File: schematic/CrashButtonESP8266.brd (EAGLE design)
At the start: 152.4 x 102.6 mm, 15 parts, among them U1 ESP12E_DEVKIT

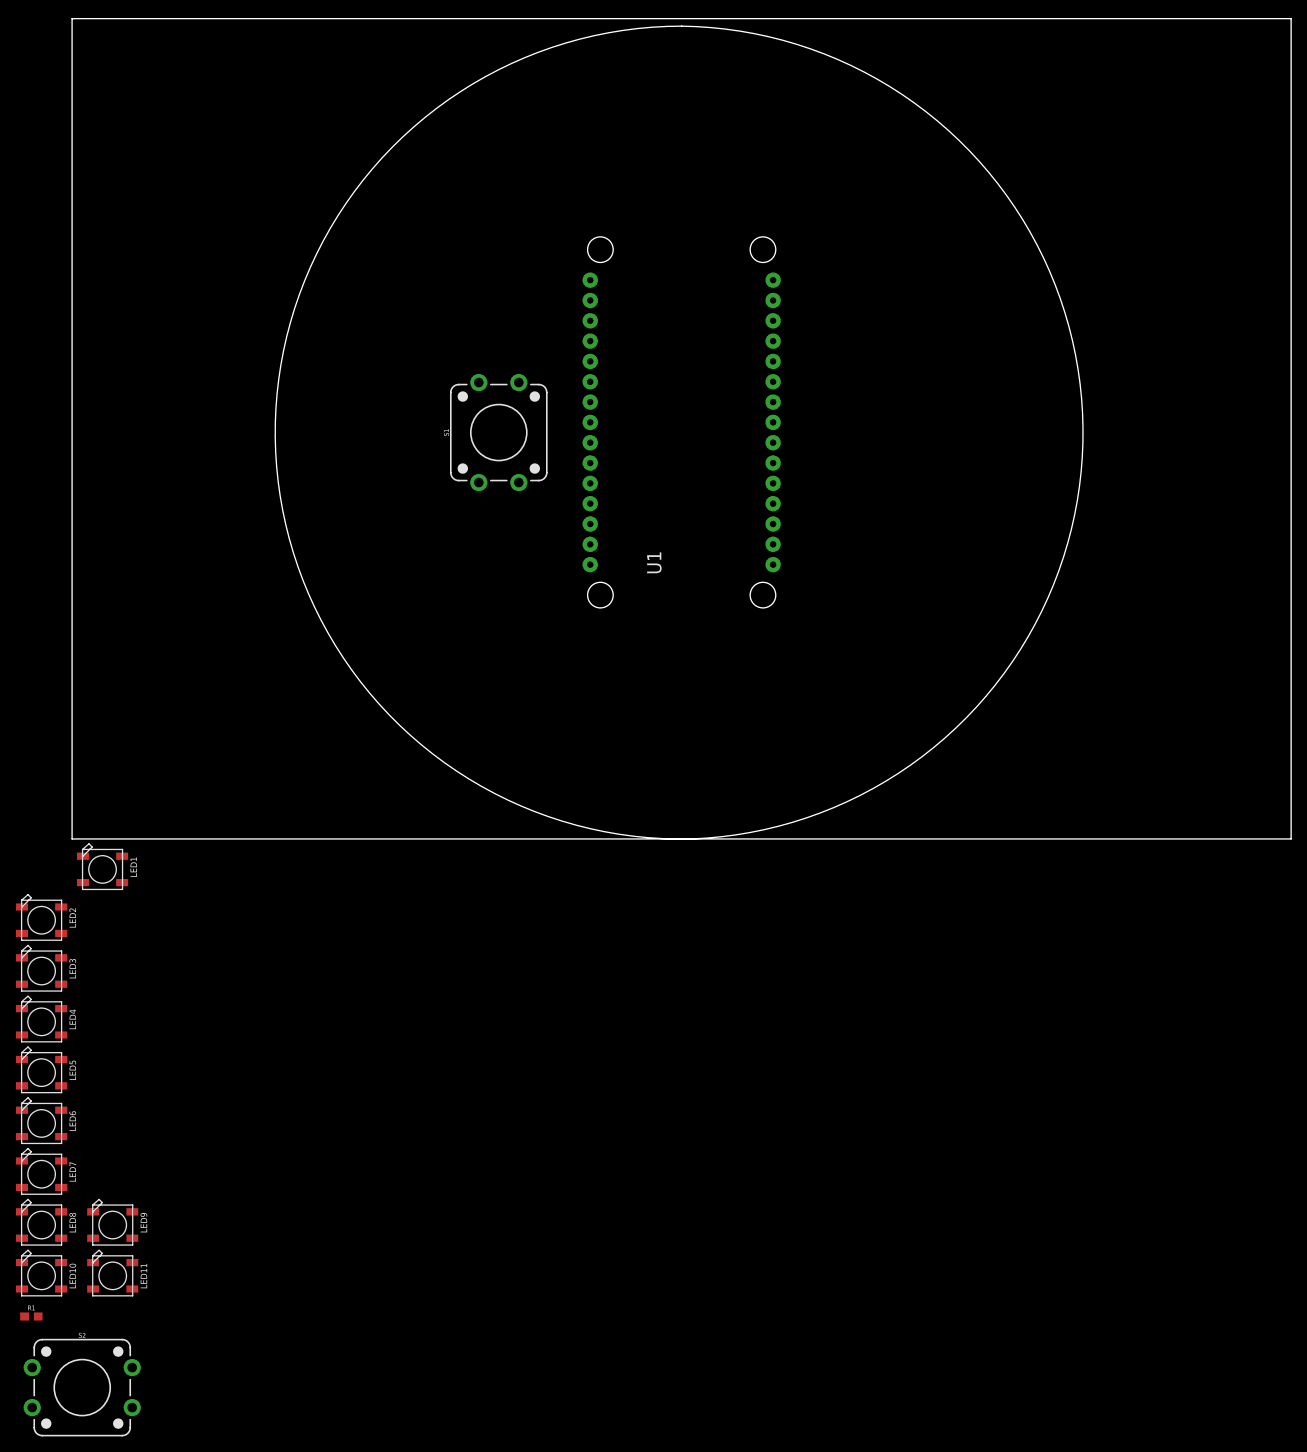
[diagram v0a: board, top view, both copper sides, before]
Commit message: circular layout
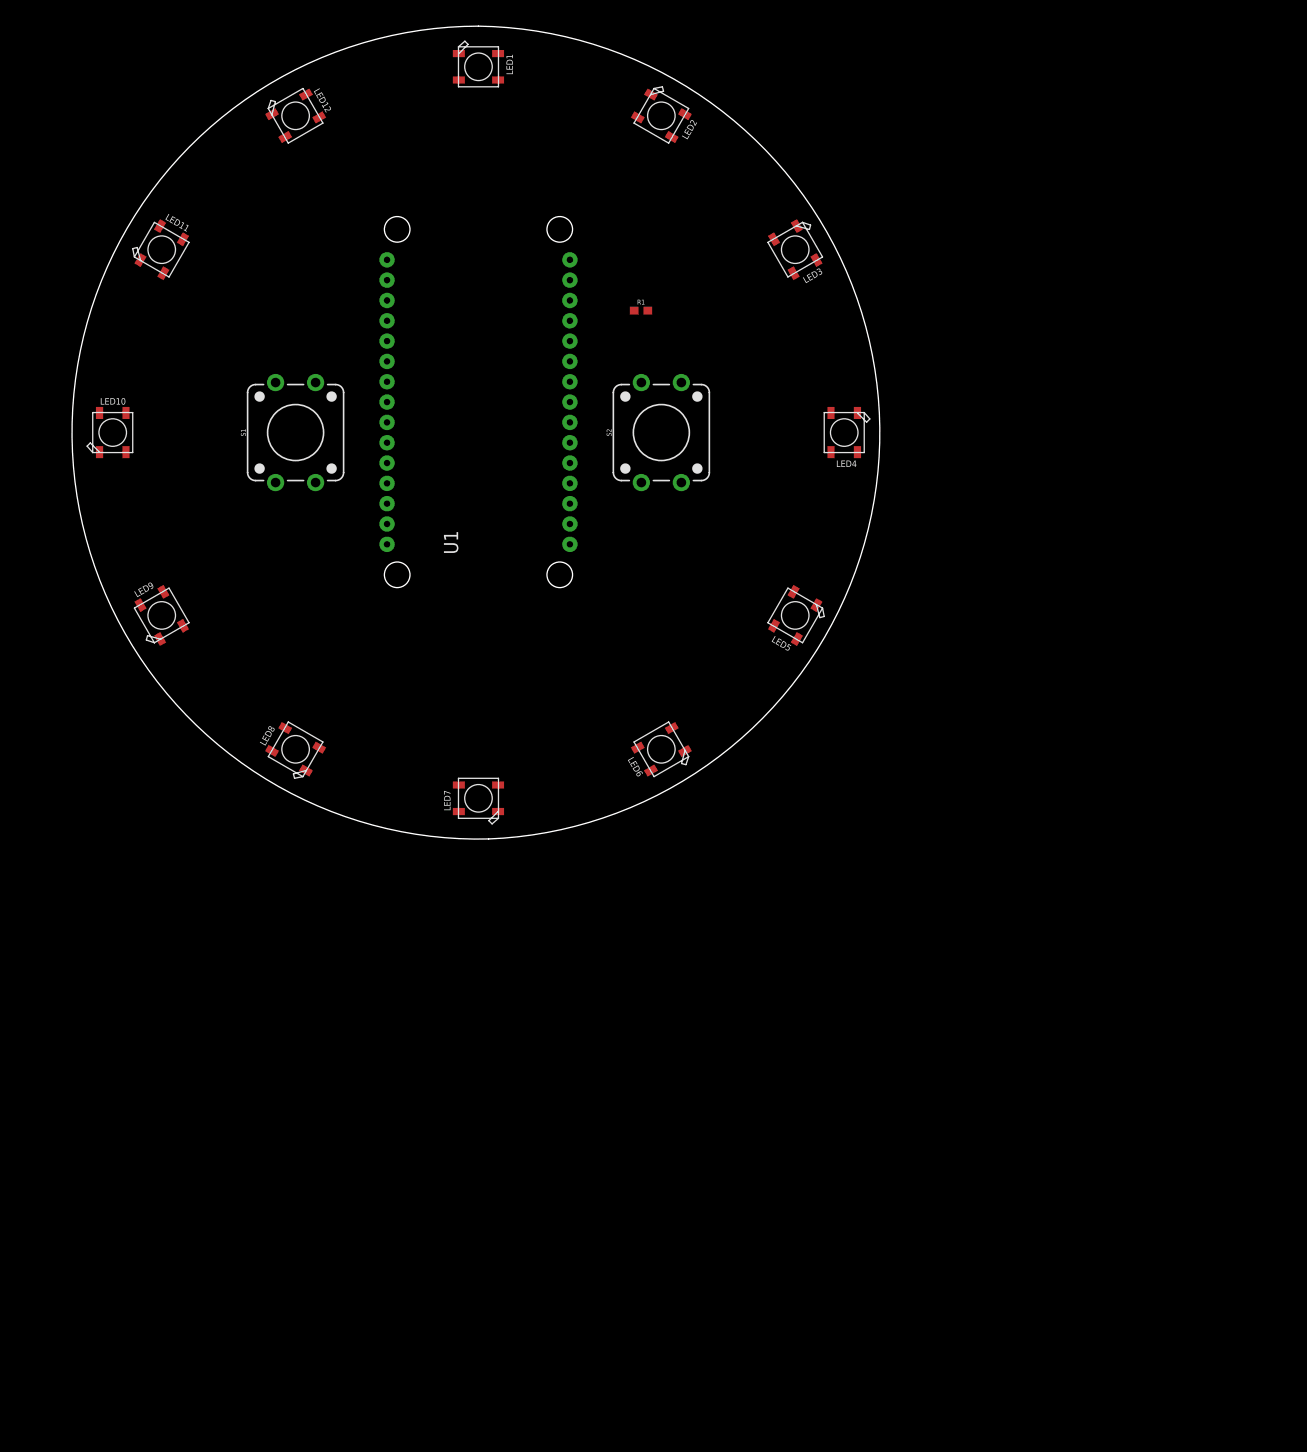
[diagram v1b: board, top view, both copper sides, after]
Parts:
- added LED12: WS2812B5050, adafruit:WS2812B
- moved R1 147.0 mm to (71.1, 66.0)
- moved S2 139.6 mm to (73.7, 50.8), turned to 90 degrees
- moved LED3 130.4 mm to (90.4, 73.7), turned to 300 degrees
- moved LED11 128.4 mm to (11.2, 73.7), turned to 60 degrees
- moved LED2 126.9 mm to (73.7, 90.4), turned to 330 degrees
- moved LED4 124.5 mm to (96.5, 50.8), turned to 270 degrees
- moved LED1 110.8 mm to (50.8, 96.5)
- moved LED5 110.2 mm to (90.4, 27.9), turned to 240 degrees
- moved LED10 105.8 mm to (5.08, 50.8), turned to 90 degrees
- moved LED6 90.5 mm to (73.7, 11.2), turned to 210 degrees
- moved LED9 76.4 mm to (11.2, 27.9), turned to 120 degrees
- moved LED7 72.0 mm to (50.8, 5.08), turned to 180 degrees
- moved LED8 67.4 mm to (27.9, 11.2), turned to 150 degrees
- moved U1 25.5 mm to (50.8, 54.6)
- moved S1 25.4 mm to (27.9, 50.8)
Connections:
- net 5V: now also LED12.1-VDD
- net GND: now also LED12.3-GND
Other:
- board size 152.4 x 102.6 mm -> 101 x 101.6 mm

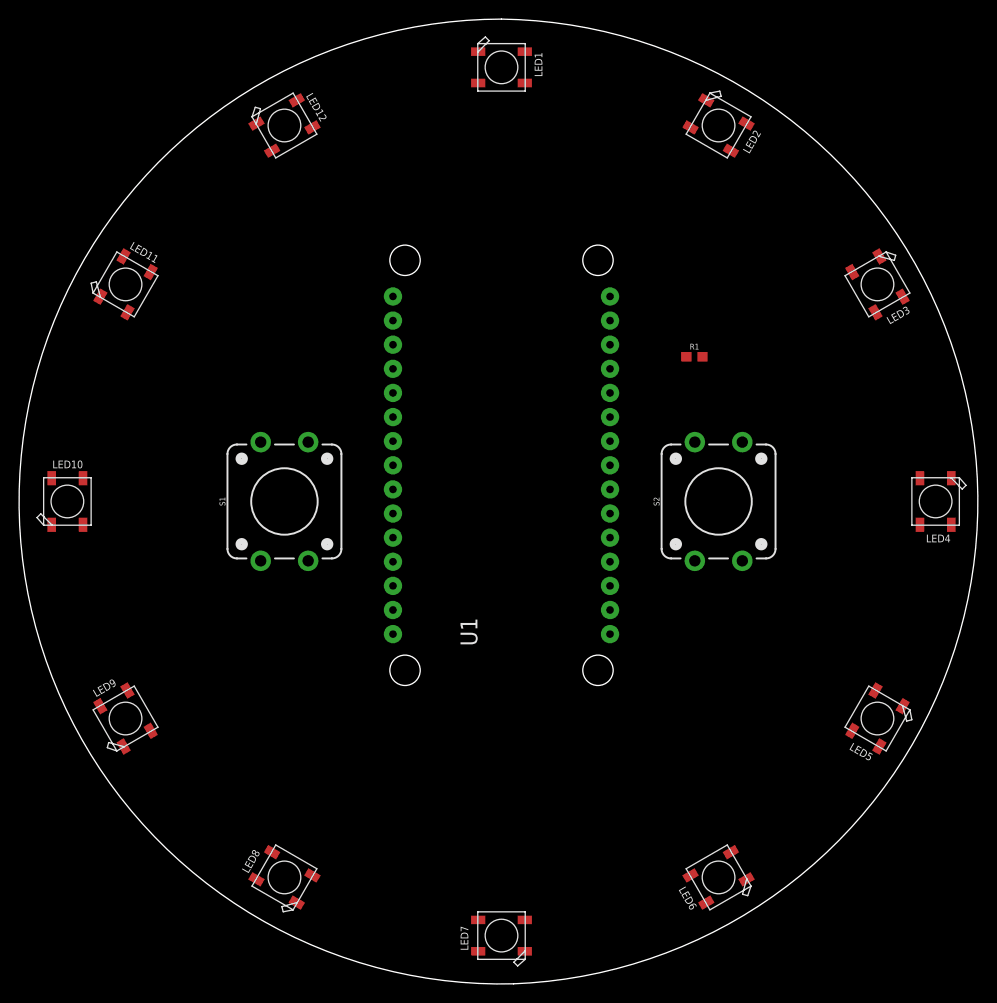
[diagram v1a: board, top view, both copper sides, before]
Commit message: moved buttoncheck to ledticker, moved ledpin to D4 in case I want to use NeoPixelBus
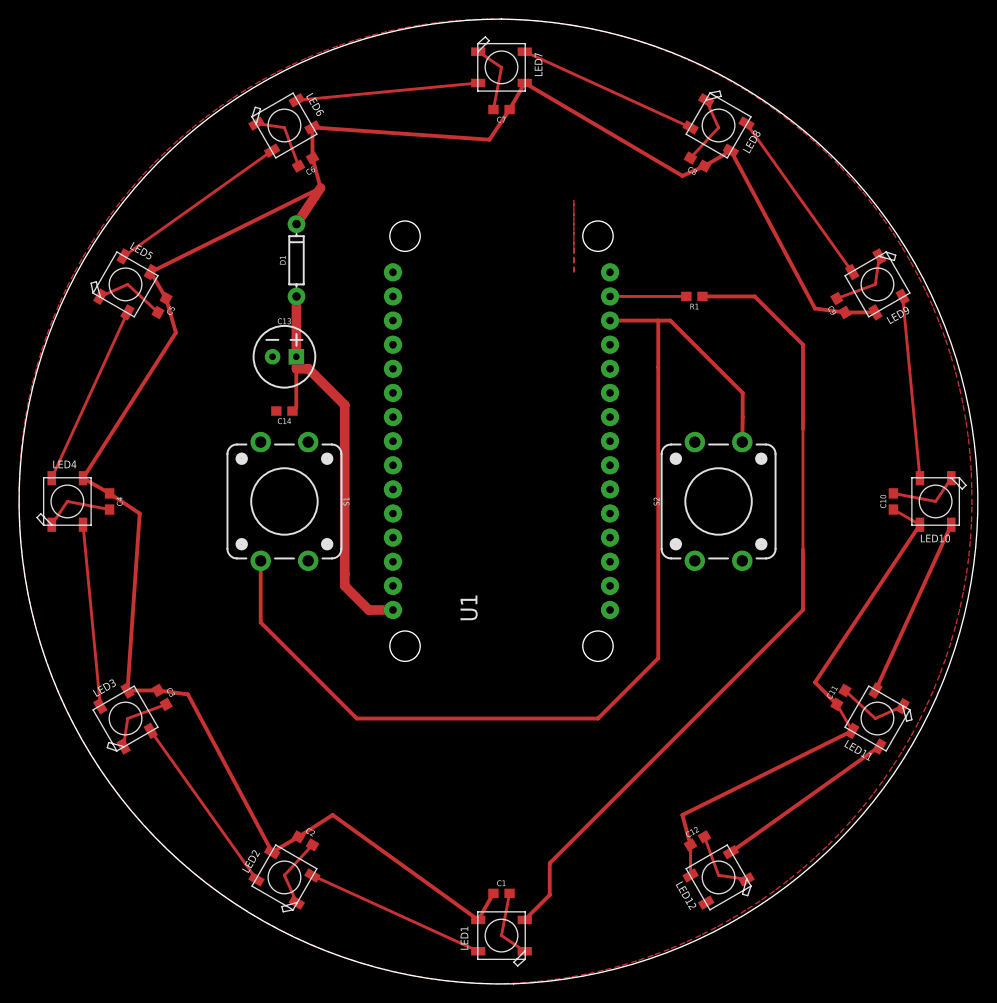
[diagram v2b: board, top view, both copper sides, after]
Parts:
- added C1, C10, C11, C12, C14, C2, C3, C4, C5, C6, C7, C8, C9: 0.1uF, SparkFun-Capacitors:0603
- added C13: 330uF, SparkFun-Capacitors:CPOL-RADIAL-2.5MM-6.5MM
- added D1: 200mA/100V/1V, SparkFun-DiscreteSemi:DIODE-1N4148
- moved LED11 91.4 mm to (90.4, 27.9), turned to 240 degrees
- moved LED12 91.4 mm to (73.7, 11.2), turned to 210 degrees
- moved LED2 91.4 mm to (27.9, 11.2), turned to 150 degrees
- moved LED3 91.4 mm to (11.2, 27.9), turned to 120 degrees
- moved LED5 91.4 mm to (11.2, 73.7), turned to 60 degrees
- moved LED6 91.4 mm to (27.9, 90.4), turned to 30 degrees
- moved LED8 91.4 mm to (73.7, 90.4), turned to 330 degrees
- moved LED9 91.4 mm to (90.4, 73.7), turned to 300 degrees
- moved LED1 91.4 mm to (50.8, 5.08), turned to 180 degrees
- moved LED10 91.4 mm to (96.5, 50.8), turned to 270 degrees
- moved LED4 91.4 mm to (5.08, 50.8), turned to 90 degrees
- moved LED7 91.4 mm to (50.8, 96.5), turned to 0 degrees
- moved R1 6.35 mm to (71.1, 72.4), turned to 180 degrees
- moved U1 2.54 mm to (50.8, 57.1)
- turned S1 to 270 degrees
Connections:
- new net N$12: LED7.2-DOUT, LED8.4-DIN
- new net N$13: LED11.2-DOUT, LED12.4-DIN
- new net N$14: C13.1, C14.1, D1.A, U1.VIN
- new net VCC: C1.1, C2.1, C3.1, C4.1, C5.1, C6.1, C7.1, C8.1, C9.1, D1.C, LED1.1-VDD, LED2.1-VDD, LED3.1-VDD, LED4.1-VDD, LED5.1-VDD, LED6.1-VDD, LED7.1-VDD, LED8.1-VDD, LED9.1-VDD
- net 5V: now also C10.1, C11.1, C12.1; no longer LED1.1-VDD, LED2.1-VDD, LED3.1-VDD, LED4.1-VDD, LED5.1-VDD, LED6.1-VDD, LED7.1-VDD, LED8.1-VDD, LED9.1-VDD, U1.VIN
- net GND: now also C1.2, C10.2, C11.2, C12.2, C13.2, C14.2, C2.2, C3.2, C4.2, C5.2, C6.2, C7.2, C8.2, C9.2
- net LEDDIN: now also R1.1
- net N$10: now also U1.D2
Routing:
- net VCC: track 0.00 -> 212.7 mm
- net N$10: track 0.00 -> 113.8 mm
- net GND: track 0.00 -> 89.1 mm
- net LEDDIN: track 0.00 -> 85.4 mm
- net 5V: track 0.00 -> 56.1 mm
- net N$14: track 0.00 -> 45.3 mm
- net N$5: track 0.00 -> 19.2 mm
- net N$2: track 0.00 -> 19.2 mm
- net N$7: track 0.00 -> 19.2 mm
- net N$13: track 0.00 -> 19.2 mm
- net N$6: track 0.00 -> 19.2 mm
- net N$3: track 0.00 -> 19.2 mm
- net N$9: track 0.00 -> 19.2 mm
- net N$1: track 0.00 -> 19.2 mm
- net N$8: track 0.00 -> 19.2 mm
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- added copper zone on layer 1, net GND
- added copper zone on layer 1, net N$15

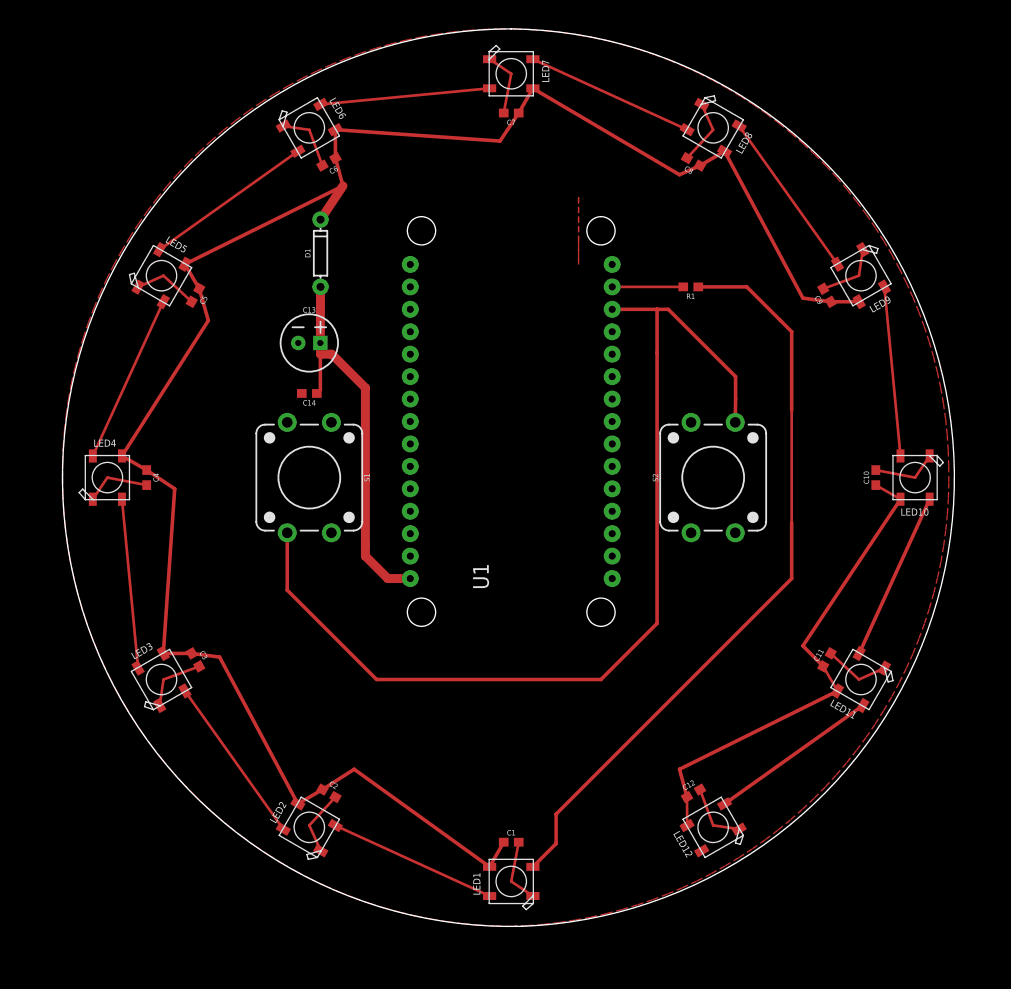
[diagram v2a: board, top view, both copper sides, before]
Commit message: version with enough polygon isolate to be solderable when othermilled
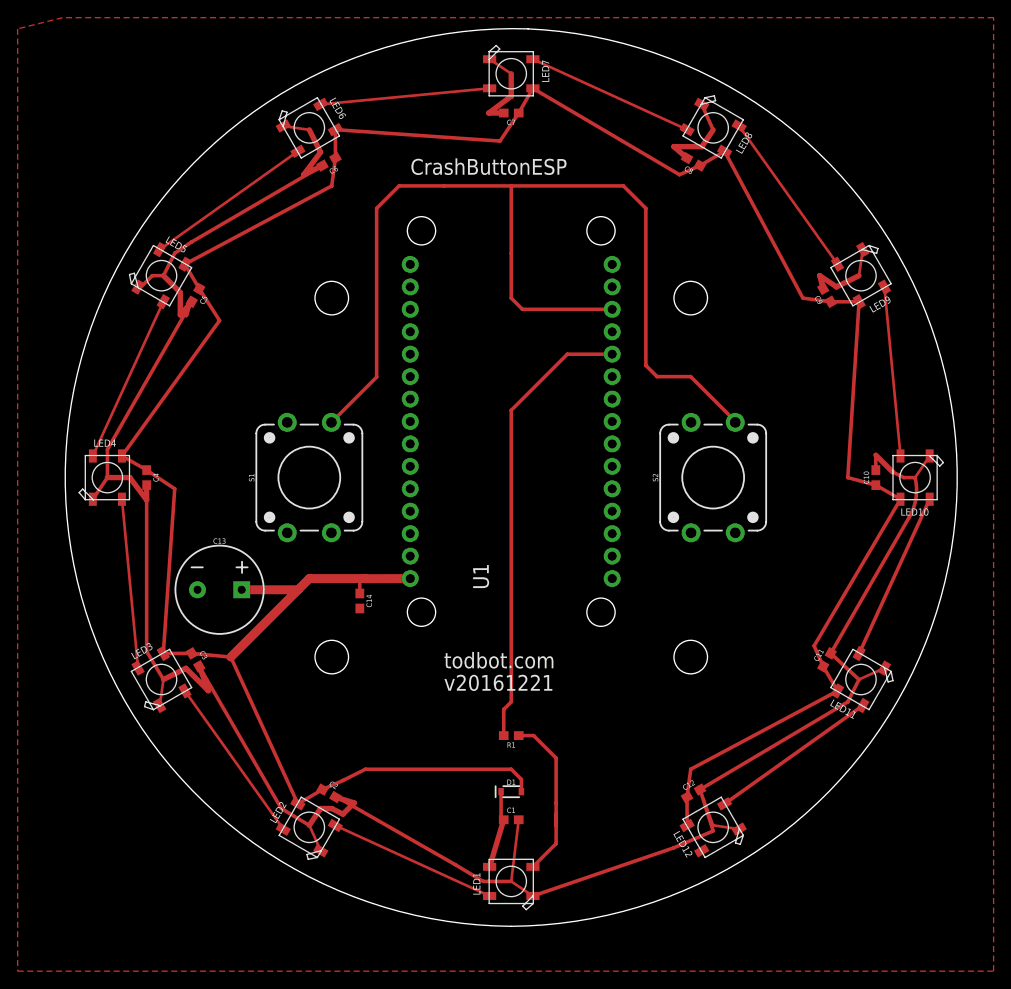
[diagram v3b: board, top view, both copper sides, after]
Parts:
- C13: value 330uF -> 1mF; device SparkFun-Capacitors:CPOL-RADIAL-2.5MM-6.5MM -> SparkFun-Capacitors:CPOL-RADIAL-5MM-10MM
- D1: value 200mA/100V/1V -> 250mA/100V; device SparkFun-DiscreteSemi:DIODE-1N4148 -> SparkFun-DiscreteSemi:SOD-323
- moved D1 64.7 mm to (50.8, 15.2), turned to 0 degrees
- moved R1 54.7 mm to (50.8, 21.6)
- moved C13 29.7 mm to (17.8, 38.1)
- moved C14 24.2 mm to (33.7, 36.8), turned to 270 degrees
- moved C1 2.54 mm to (50.8, 12.1)
- turned S1 to 90 degrees
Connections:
- removed net 5V: C10.1, C11.1, C12.1, LED10.1-VDD, LED11.1-VDD, LED12.1-VDD
- removed net N$14: C13.1, C14.1, D1.A, U1.VIN
- new net VIN: C10.1, C11.1, C12.1, C13.+, C14.1, C2.1, C3.1, C4.1, C5.1, C6.1, C7.1, C8.1, C9.1, D1.A, LED10.1-VDD, LED11.1-VDD, LED12.1-VDD, LED2.1-VDD, LED3.1-VDD, LED4.1-VDD, LED5.1-VDD, LED6.1-VDD, LED7.1-VDD, LED8.1-VDD, LED9.1-VDD, U1.VIN
- net GND: now also C13.-; no longer C13.2
- net N$11: now also U1.D4; no longer U1.D1
- net VCC: no longer C2.1, C3.1, C4.1, C5.1, C6.1, C7.1, C8.1, C9.1, LED2.1-VDD, LED3.1-VDD, LED4.1-VDD, LED5.1-VDD, LED6.1-VDD, LED7.1-VDD, LED8.1-VDD, LED9.1-VDD
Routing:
- net VIN: track 0.00 -> 316.8 mm
- net GND: track 89.1 -> 312.4 mm
- net VCC: track 212.7 -> 9.04 mm
- net LEDDIN: track 85.4 -> 20.0 mm
- net 5V: track 56.1 -> 0.00 mm
- net N$14: track 45.3 -> 0.00 mm
- net N$11: track 8.04 -> 51.2 mm
- net N$10: track 113.8 -> 115.0 mm
- removed copper zone on layer 1, net N$15
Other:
- outline, holes or cut-outs redrawn
- board text added: "CrashButtonESP"
- board text added: "todbot.com"
- board text added: "v20161221"
